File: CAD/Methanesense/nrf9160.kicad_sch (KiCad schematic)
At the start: 40 parts, among them J3 Conn_Coaxial, J4 Conn_Coaxial, J5 SIM_Card, J6 Conn_02x05_Odd_Even, J7 Conn_02x05_Odd_Even, Q2 FDS6892A, SW1 KMR223GLFG, SW2 JS202011JCQN, U6 nRF9161-SIXX, U8 USBLC6-4SC6, U9 TPS22917DBV

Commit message: WIP
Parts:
- removed J3: Conn_Coaxial, Connector_Coaxial:U.FL_Hirose_U.FL-R-SMT-1_Vertical, symbol Connector:Conn_Coaxial
- removed J5: SIM_Card, Connector_Card:microSIM_JAE_SF53S006VCBR2000, symbol Connector:SIM_Card
- removed R27: 120R, symbol Library:R
- removed U6: nRF9161-SIXX, PCM_nordic-lib-kicad-nrf9:LGA_9161_16.0x10.5mm, symbol PCM_nordic-lib-kicad-nrf9:nRF9161-SIXX
- added AE1: NN02-220, symbol Device:Antenna
- added AE2: YCGO009AA, symbol Device:Antenna
- added C1, C2: 1.7pF, Methanesense:C_0603_1608Metric, symbol Device:C
- added C4: 8.5pF, Methanesense:C_0603_1608Metric, symbol Device:C
- added C5: 15pF, Methanesense:C_0603_1608Metric, symbol Device:C
- added J2: Conn_Coaxial, Connector_Coaxial:U.FL_Hirose_U.FL-R-SMT-1_Vertical, symbol Connector:Conn_Coaxial
- added J3: 693043020611, Methanesense:693043020611, symbol 693043020611:693043020611
- added L1: 2.3nH, Methanesense:L_0603_1608Metric, symbol Device:L
- added L4: NP, Methanesense:L_0603_1608Metric, symbol Device:L
- added L5: 7.5NH, Methanesense:L_0603_1608Metric, symbol Device:L
- added L6: 1.6nH, Methanesense:L_0603_1608Metric, symbol Device:L
- added L7: 39NH, Methanesense:L_0603_1608Metric, symbol Device:L
- added L8: 68 nH, Methanesense:L_0603_1608Metric, symbol Device:L
- added R12, R13: 10k, Resistor_SMD:R_0603_1608Metric, symbol Library:R
- added U5: nRF9160-SICA, PCM_nordic-lib-kicad-nrf9:LGA_9160_16.0x10.5mm, symbol PCM_nordic-lib-kicad-nrf9:nRF9160-SIXX
- C21, C22: footprint (none) -> Capacitor_SMD:C_0805_2012Metric
- C23, C24, C25, C28, C29, C30, C31, C32, C33, C34, C35, C36, R18, R19, R20, R22, R23, R26: footprint (none) -> Capacitor_SMD:C_0603_1608Metric
- C26, C27: footprint (none) -> Methanesense:C_0603_1608Metric
- D5, D6: footprint (none) -> LED_SMD:LED_0603_1608Metric
- J6: value Conn_02x05_Odd_Even -> JLINK; footprint Connector_PinHeader_1.27mm:PinHeader_2x05_P1.27mm_Vertical_SMD -> esprelay:SEXY_pinpogo
- L2: value 39NH 250MA 0.7OHM SMD -> 39NH; footprint (none) -> Methanesense:L_0603_1608Metric
- R17, R24, R25: footprint (none) -> Resistor_SMD:R_0603_1608Metric
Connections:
- net ANT: now also C5.1, U5.61 (ANT)
- net COEX0: now also U5.93 (COEX0)
- net GND: now also C2.2, J2.2 (Ext), J3.C5 (GND), J3.S1, J3.S2, J3.S3, J3.S4, J3.S5, J3.S6, L4.2, L5.2, L7.2, U5.1 (GND_Shield), U5.103 (VSS), U5.11 (GND_Shield), U5.14 (GND_Shield), U5.17 (GND_Shield), U5.21 (GND_Shield), U5.27 (GND_Shield), U5.31 (GND_Shield), U5.36 (GND_Shield), U5.41 (GND_Shield), U5.44 (GND_Shield), U5.47 (GND_Shield), U5.5 (GND_Shield), U5.50 (GND_Shield), U5.52 (GND_Shield), U5.56 (GND_Shield), U5.6 (GND_Shield), U5.60 (GND_Shield), U5.62 (GND_Shield), U5.63 (GND_Shield), U5.65 (GND_Shield), U5.66 (GND_Shield), U5.68 (GND_Shield), U5.69 (GND_Shield), U5.7 (GND_Shield), U5.72 (GND_Shield), U5.74 (GND_Shield), U5.75 (GND_Shield), U5.76 (GND_Shield), U5.77 (GND_Shield), U5.78 (GND_Shield), U5.79 (GND_Shield), U5.8 (GND_Shield), U5.80 (GND_Shield), U5.81 (GND_Shield), U5.82 (GND_Shield), U5.85 (GND_Shield), U5.9 (GND_Shield), U5.90 (GND_Shield), U5.94 (GND_Shield), U5.98 (GND_Shield)
- net GPS: now also U5.67 (GPS)
- net P0.05: now also U5.2 (P0.05)
- net P0.06: now also U5.3 (P0.06)
- net P0.07: now also U5.4 (P0.07)
- net P0.08: now also U5.15 (P0.08)
- net P0.31: now also U5.89 (P0.31)
- net SIM_CLK: now also U5.46 (SIM_CLK)
- net SIM_IO: now also U8.1 (I/O1), U5.48 (SIM_IO); no longer U8.4 (I/O3)
- net SIM_RST: now also U8.4 (I/O3), U5.43 (SIM_RST); no longer U8.1 (I/O1)
- net SWDCLK: now also U5.33 (SWDCLK)
- net SWDIO: now also U5.34 (SWDIO)
- net SWO: now also U5.95 (P0.00)
- net ~{RESET}: now also U5.32 (~{RESET})
- net at C25.1: now also U5.13 (DEC0)
- net at R20.1: now also J3.C7 (I/O)
- net at R18.1: now also J3.C2 (RST)
- net at R19.1: now also J3.C3 (CLK)
- net +1V8 renamed +1V8SIM
- net +1V8SIM: now also J3.C1 (VCC), U5.49 (SIM_1V8)
- net ANT-: no longer names the net of C27.2, L2.1
- net ANT-: now also C1.1
- net GPS-: no longer names the net of C29.1, U9.6 (VOUT)
- net GPS-: now also L8.2; no longer C30.2, J4.1 (In)
- net QOD: no longer names the net of U9.5 (QOD)
- net VCC renamed +5V
- net +5V: now also U5.101 (ENABLE), U5.102 (VDD1), U5.22 (VDD2); no longer C23.1, C36.1
- net VDD renamed +2V0
- net +2V0: now also C23.1, C36.1, R12.2, R13.2, U5.12 (VDD_GPIO)
- new net: C1.2, L1.1
- new net: C2.1, C4.1, L1.2, L4.1
- new net: C5.2, J2.1 (In), L7.1
- new net: AE1.1 (A), L6.2
- new net: C4.2, L5.1, L6.1
- new net GPS_: C30.2, J4.1 (In), L8.1
- new net SCL: R13.1
- new net SDA: R12.1
- no-connect marks 15 -> 22
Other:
- moved on the sheet: C26, C27, C29, J6, L2

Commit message: Allmost there
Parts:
- removed R12, R13: 10k, Resistor_SMD:R_0603_1608Metric, symbol Library:R
- AE1: footprint (none) -> Methanesense:XCVR_NN02-220
- J6: now not fitted

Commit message: WIP
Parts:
- removed J7: Conn_02x05_Odd_Even, Connector_PinHeader_2.54mm:PinHeader_2x05_P2.54mm_Vertical, symbol Connector_Generic:Conn_02x05_Odd_Even
- added J5: Conn_01x10_Pin, Connector_PinHeader_2.54mm:PinHeader_1x10_P2.54mm_Vertical, symbol Connector:Conn_01x10_Pin
- C1, C2: MPN (none) -> GJM1555C1H1R7WB01
- C26, C27, C5: footprint Methanesense:C_0603_1608Metric -> Methanesense:C_0402_1005Metric_Sqr
- C29, C30: footprint Capacitor_SMD:C_0603_1608Metric -> Methanesense:C_0402_1005Metric_Sqr
- C4: MPN (none) -> GJM1555C1H8R5WB01
- J2, J4: MPN (none) -> HIROSE ELECTRIC U.FL-R-SMT-1
- J3: MPN (none) -> 693043020611
- L1: MPN (none) -> LQW15AN2N3G80
- L2, L7, L8: footprint Methanesense:L_0603_1608Metric -> Methanesense:C_0402_1005Metric_Sqr
- L5: MPN (none) -> LQW15AN7N5G80
- L6: MPN (none) -> LQW15AN1N6C80
- SW1: MPN (none) -> KMR223GLFG
- SW2: MPN (none) -> JS202011JCQN
- U5: MPN (none) -> nRF9160-SICA
- U8: MPN (none) -> USBLC6-4SC6
- U9: MPN (none) -> TPS22917DBV
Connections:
- net +2V0: now also J5.1 (Pin_1)
- net +5V: now also J5.2 (Pin_2)
- net +BATT: now also J5.3 (Pin_3)
- net GND: now also J5.4 (Pin_4), J5.6 (Pin_6)
- net P0.05: now also J5.9 (Pin_9)
- net P0.06: now also J5.8 (Pin_8)
- net P0.07: now also J5.7 (Pin_7)
- net P0.08: now also J5.10 (Pin_10)
- net P0.04: now reaches U5.100 (P0.04)
- net P0.09: now reaches U5.16 (P0.09)
- net P0.10: now reaches U5.18 (P0.10)
- net P0.11: now reaches U5.19 (P0.11)
- net P0.12: now reaches U5.20 (P0.12)
- net P0.13/AIN0: now reaches U5.23 (P0.13/AIN0)
- net P0.14/AIN1: now reaches U5.24 (P0.14/AIN1)
- net P0.15/AIN2: now reaches U5.25 (P0.15/AIN2)
- net P0.16/AIN3: now reaches U5.26 (P0.16/AIN3)
- net P0.17/AIN4: now reaches U5.28 (P0.17/AIN4)
- net P0.18/AIN5: now reaches U5.29 (P0.18/AIN5)
- net P0.19/AIN6: now reaches U5.30 (P0.19/AIN6)
- net P0.20/AIN7: now reaches U5.35 (P0.20/AIN7)
- net P0.26: now reaches U5.83 (P0.26)
- net P0.27: now reaches U5.84 (P0.27)
- net P0.28: now reaches U5.86 (P0.28)
- net P0.29: now reaches U5.87 (P0.29)
- net P0.30: now reaches U5.88 (P0.30)
- net P0.01: now reaches U5.96 (P0.01)
- net P0.02: now reaches U5.97 (P0.02)
- net P0.03: now reaches U5.99 (P0.03)
- new net +5VL: J5.5 (Pin_5)
- no-connect marks 22 -> 21
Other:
- moved on the sheet: C24, C28, R17

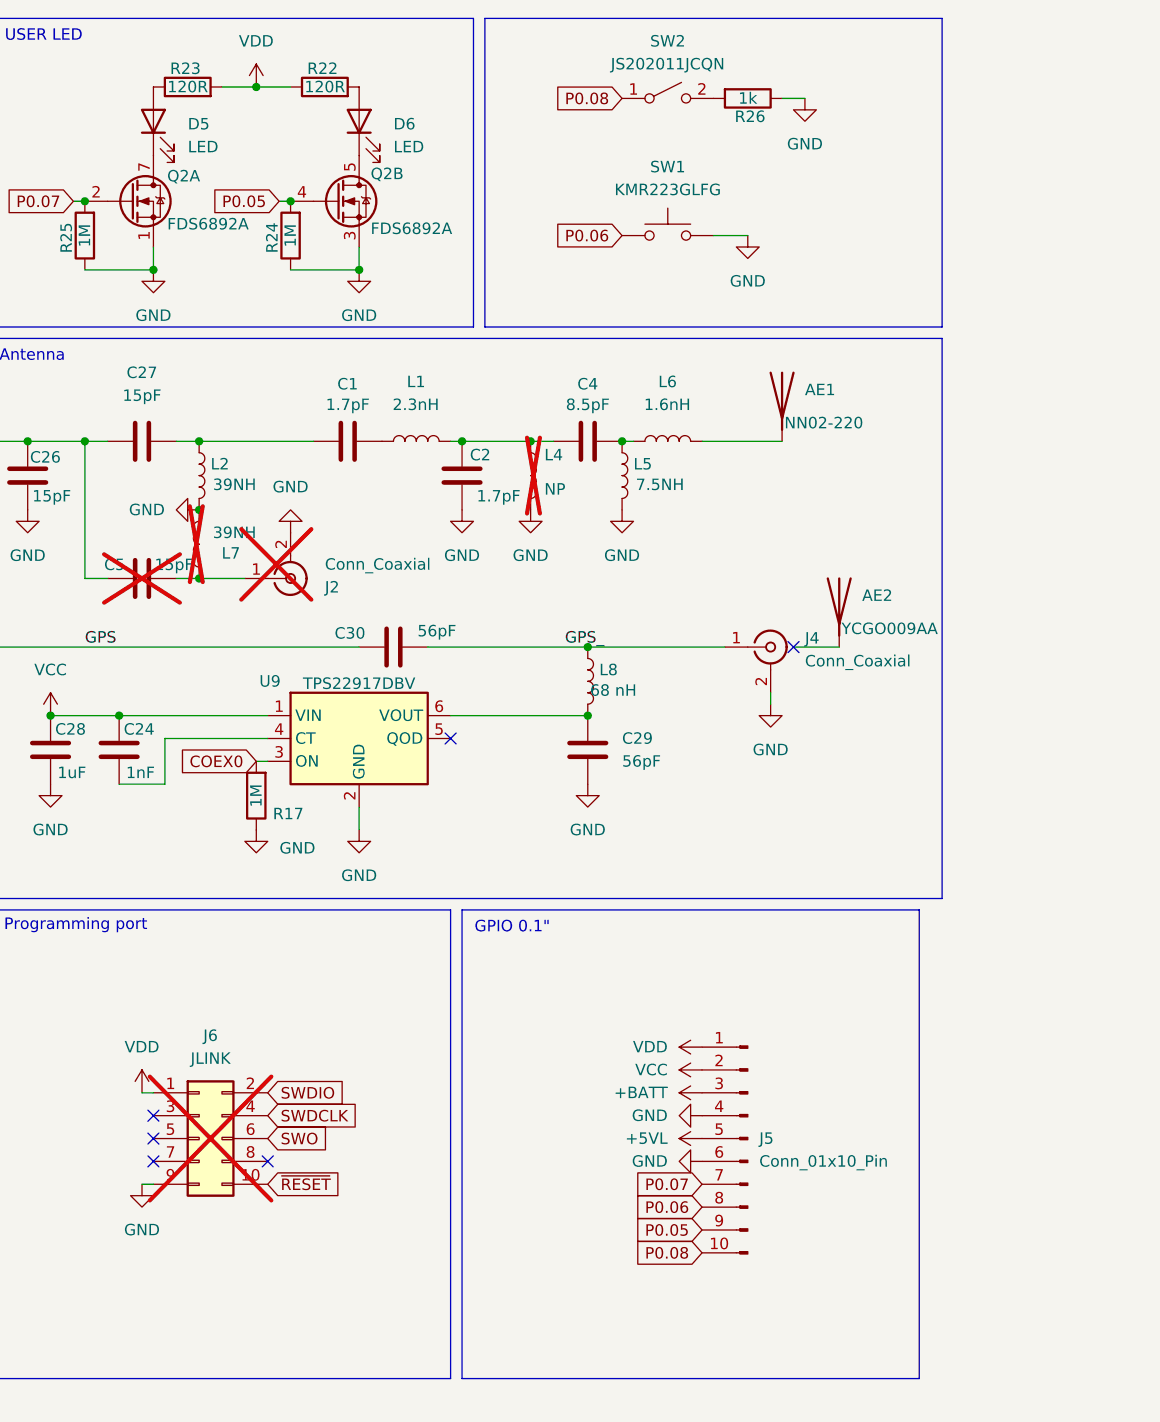
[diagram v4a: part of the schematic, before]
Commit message: NRF footprint change
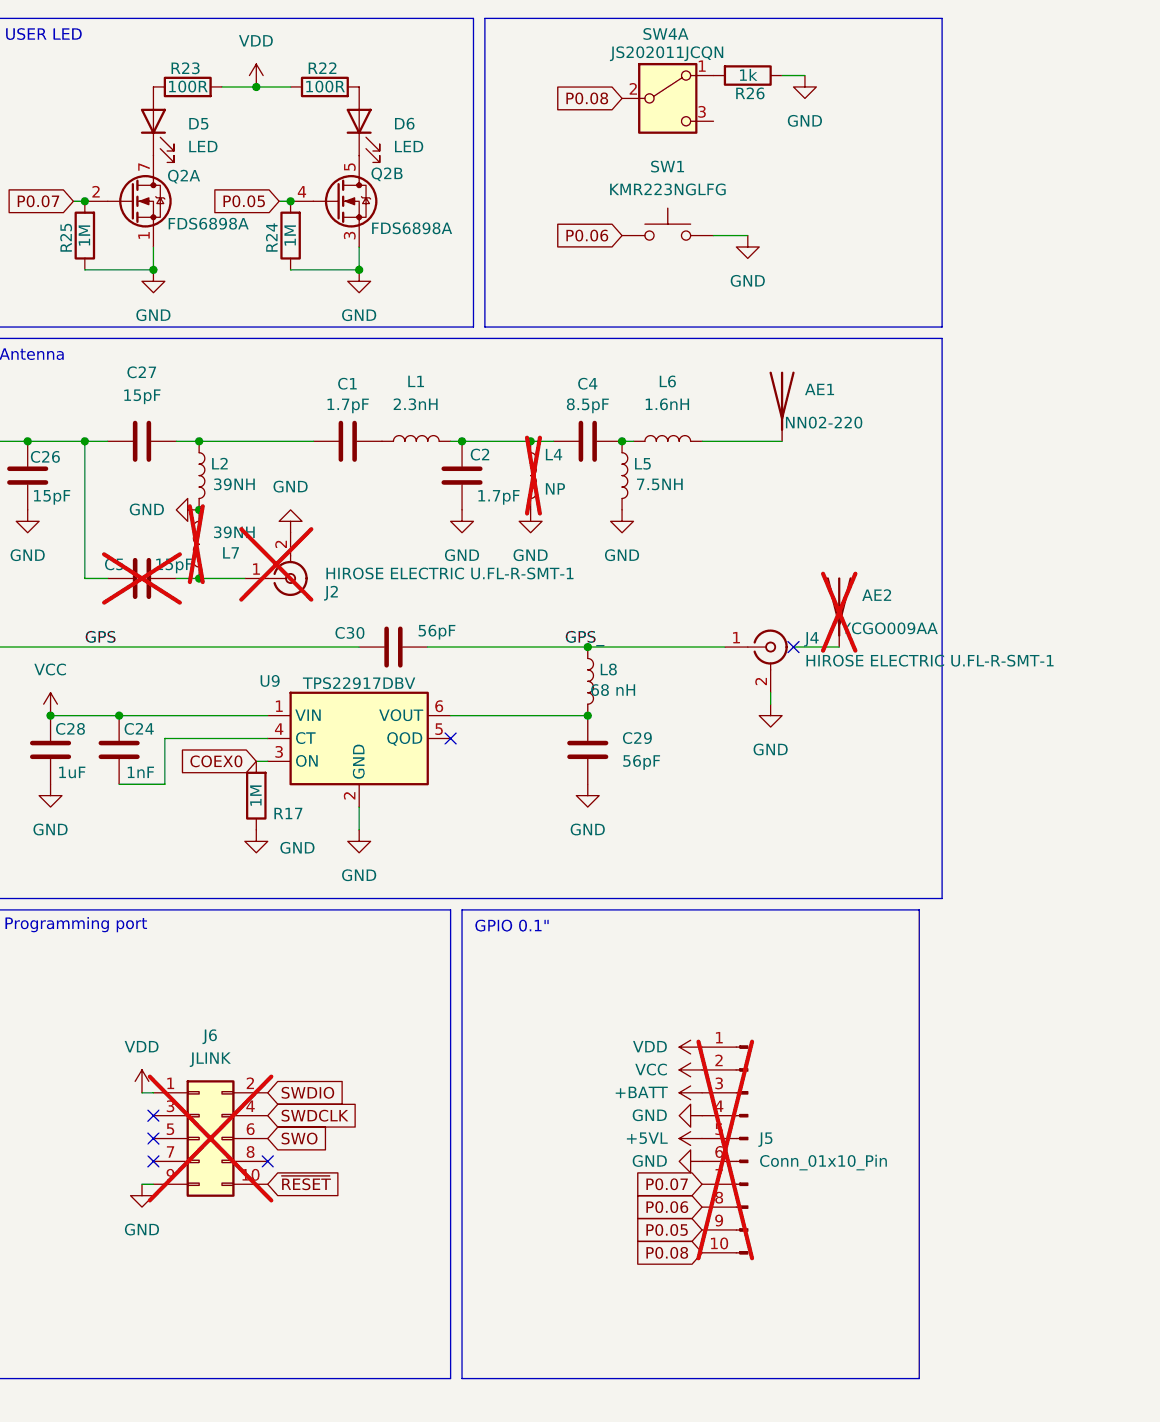
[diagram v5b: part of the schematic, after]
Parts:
- removed SW2: JS202011JCQN, Button_Switch_SMD:SW_DIP_SPSTx01_Slide_6.7x4.1mm_W6.73mm_P2.54mm_LowProfile_JPin, symbol Switch:SW_SPST
- added SW4: JS202011JCQN, Button_Switch_SMD:SW_DPDT_CK_JS202011JCQN, symbol Switch:SW_DPDT_x2
- AE1: MPN (none) -> NN02-220
- AE2, J5: now not fitted
- C26, C27, C5: MPN (none) -> GJM0335C1E150GB01D
- C29, C30: MPN (none) -> CBR04C560F1GAC
- C33, C35: footprint Capacitor_SMD:C_0603_1608Metric -> Methanesense:C_0402_1005Metric_Sqr; MPN (none) -> GJM0335C1E150GB01D
- D5, D6: MPN (none) -> LG L29K-G2J1-24-Z
- J2, J4: value Conn_Coaxial -> HIROSE ELECTRIC U.FL-R-SMT-1; footprint Connector_Coaxial:U.FL_Hirose_U.FL-R-SMT-1_Vertical -> Methanesense:U.FL_Hirose_U.FL-R-SMT-1_Vertical; MPN HIROSE ELECTRIC U.FL-R-SMT-1 -> U.FL-R-SMT-1
- J3: Package None -> (none)
- L2, L7: MPN (none) -> LQW15AN39NJ8ZD
- L8: MPN (none) -> LQW15AN68NG0ZD
- Q2: value FDS6892A -> FDS6898A; MPN (none) -> FDS6898A
- R18, R19, R20, R26: footprint Capacitor_SMD:C_0603_1608Metric -> Resistor_SMD:R_0603_1608Metric
- R22, R23: value 120R -> 100R; footprint Capacitor_SMD:C_0603_1608Metric -> Resistor_SMD:R_0603_1608Metric
- SW1: value KMR223GLFG -> KMR223NGLFG; footprint Button_Switch_SMD:SW_Push_1P1T_NO_CK_KMR2 -> Methanesense:SW_Push_1P1T_NO_CK_KMR2; MPN KMR223GLFG -> KMR223NGLFG
- U5: footprint PCM_nordic-lib-kicad-nrf9:LGA_9160_16.0x10.5mm -> Methanesense:LGA_9160_16.0x10.5mm; MPN nRF9160-SICA -> nRF9160-SICA-B1A-R7
- U9: MPN TPS22917DBV -> TPS22917DBVR
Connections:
- net P0.08: now also SW4.2 (B)
- net at R26.2: now also SW4.1 (A)
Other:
- moved on the sheet: R26

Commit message: Rev 2.0.0
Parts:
- C26, C27, C33, C35, C5: MPN GJM0335C1E150GB01D -> VJ0402D150FXCAJ
- R26, SW1, SW4: now not fitted
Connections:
- net GND: now also J6.3 (Pin_3), J6.5 (Pin_5), J6.7 (Pin_7), J6.8 (Pin_8)
- net P0.06: now also Q2.2 (G1), R25.2; no longer SW1.1
- net P0.07: now also SW1.1; no longer Q2.2 (G1), R25.2
- net P0.08: no longer J5.10 (Pin_10), SW4.2 (B)
- net P0.11: now also J5.10 (Pin_10), SW4.2 (B)
- no-connect marks 21 -> 17

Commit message: rev 1.2
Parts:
- removed C1, C2: 1.7pF, Methanesense:C_0603_1608Metric, symbol Device:C
- removed C4: 8.5pF, Methanesense:C_0603_1608Metric, symbol Device:C
- removed C5: 15pF, Methanesense:C_0402_1005Metric_Sqr, symbol Device:C
- removed D5, D6: LED, LED_SMD:LED_0603_1608Metric, symbol Device:LED
- removed J2: HIROSE ELECTRIC U.FL-R-SMT-1, Methanesense:U.FL_Hirose_U.FL-R-SMT-1_Vertical, symbol Connector:Conn_Coaxial
- removed J5: Conn_01x10_Pin, Connector_PinHeader_2.54mm:PinHeader_1x10_P2.54mm_Vertical, symbol Connector:Conn_01x10_Pin
- removed L1: 2.3nH, Methanesense:L_0603_1608Metric, symbol Device:L
- removed L4: NP, Methanesense:L_0603_1608Metric, symbol Device:L
- removed L5: 7.5NH, Methanesense:L_0603_1608Metric, symbol Device:L
- removed L6: 1.6nH, Methanesense:L_0603_1608Metric, symbol Device:L
- removed L7: 39NH, Methanesense:C_0402_1005Metric_Sqr, symbol Device:L
- removed R22, R23: 100R, Resistor_SMD:R_0603_1608Metric, symbol Library:R
- removed R26: 1k, Resistor_SMD:R_0603_1608Metric, symbol Library:R
- removed SW4: JS202011JCQN, Button_Switch_SMD:SW_DPDT_CK_JS202011JCQN, symbol Switch:SW_DPDT_x2
- added J1: HIROSE ELECTRIC U.FL-R-SMT-1, Methanesense:U.FL_Hirose_U.FL-R-SMT-1_Vertical, symbol Connector:Conn_Coaxial
- added J5: Conn_01x12_Pin, Connector_PinHeader_2.54mm:PinHeader_1x12_P2.54mm_Vertical, symbol Connector:Conn_01x12_Pin
- added R6: 0R, Resistor_SMD:R_0603_1608Metric, symbol Library:R
- AE1: value NN02-220 -> ~; footprint Methanesense:XCVR_NN02-220 -> (none); MPN NN02-220 -> (none); now not fitted
- J6, SW1: now fitted
- L8: value 68 nH -> 68 nH
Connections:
- net +2V0: now also J5.4 (Pin_4)
- net +BATT: now also J5.2 (Pin_2)
- net GND: now also J1.2 (Ext), J5.1 (Pin_1), J5.12 (Pin_12), J5.3 (Pin_3), J5.5 (Pin_5)
- net P0.01: now also Q2.4 (G2), R24.2
- net P0.04: now also SW1.1
- net P0.05: no longer Q2.4 (G2), R24.2
- net P0.06: no longer Q2.2 (G1), R25.2
- net P0.07: no longer SW1.1
- net P0.08: now also J5.6 (Pin_6)
- net P0.09: now also J5.7 (Pin_7)
- net P0.10: now also J5.8 (Pin_8)
- net P0.14/AIN1: now also J5.11 (Pin_11)
- net P0.17/AIN4: now also Q2.2 (G1), R25.2
- net P0.19/AIN6: now also J5.10 (Pin_10)
- net OD1: now reaches Q2.5 (D2), Q2.6 (D2)
- net OD2: now reaches Q2.7 (D1), Q2.8 (D1)
- net at C27.2, L2.1: now also R6.2
- net +5V renamed VCC
- net GPS: no longer names the net of C30.1, U5.67 (GPS)
- new net: J1.1 (In), R6.1
- new net P0.18/AIN5: J5.9 (Pin_9)
- no-connect marks 17 -> 18
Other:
- note added: "USER IO"
- note removed: "USER LED"
- moved on the sheet: C26, C27, L2

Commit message: Feat: Rev 1.3
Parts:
- removed J5: Conn_01x12_Pin, Connector_PinHeader_2.54mm:PinHeader_1x12_P2.54mm_Vertical, symbol Connector:Conn_01x12_Pin
- added D7: LG L29K-G2J1-24-Z, LED_SMD:LED_0603_1608Metric, symbol Device:LED
- added D8: MSS1P3L-M3/89A, Diode_SMD:D_MicroSMP_AK, symbol Device:D_Schottky
- added J5: Conn_01x13_Pin, Connector_PinHeader_2.54mm:PinHeader_1x13_P2.54mm_Vertical, symbol Connector:Conn_01x13_Pin
- added R29: 150R, Resistor_SMD:R_0603_1608Metric, symbol Library:R
- added R31, R32, R33: 0R, Resistor_SMD:R_0402_1005Metric, symbol Library:R
- added TP1: SWDIO, TestPoint:TestPoint_Pad_D1.0mm, symbol Connector:TestPoint
- added TP15: GND, TestPoint:TestPoint_Pad_D1.0mm, symbol Connector:TestPoint
- added TP2: SWDCLK, TestPoint:TestPoint_Pad_D1.0mm, symbol Connector:TestPoint
- added TP3: SWO, TestPoint:TestPoint_Pad_D1.0mm, symbol Connector:TestPoint
- added TP4: RST, TestPoint:TestPoint_Pad_D1.0mm, symbol Connector:TestPoint
- J6: MPN (none) -> BD125-10-A-0305-0580-L-B
- R6: footprint Resistor_SMD:R_0603_1608Metric -> Resistor_SMD:R_0402_1005Metric
- SW1: MPN KMR223NGLFG -> KMR223GLFG
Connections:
- net +2V0: now also J5.4 (Pin_4)
- net +BATT: now also J5.2 (Pin_2)
- net GND: now also D7.1 (K), J5.1 (Pin_1), J5.12 (Pin_12), J5.3 (Pin_3), J5.5 (Pin_5), R31.2, R32.2, TP15.1
- net P0.06: now also R29.2
- net P0.08: now also J5.6 (Pin_6)
- net P0.09: now also J5.7 (Pin_7)
- net P0.10: now also J5.8 (Pin_8)
- net P0.14/AIN1: now also J5.11 (Pin_11)
- net P0.18/AIN5: now also J5.9 (Pin_9)
- net P0.19/AIN6: now also J5.10 (Pin_10)
- net SWDCLK: now also TP2.1
- net SWDIO: now also TP1.1
- net SWO: now also TP3.1
- net ~{RESET}: now also TP4.1
- net at R6.1: now also R31.1, R33.1; no longer J1.1 (In)
- new net: D7.2 (A), R29.1
- new net: J1.1 (In), R32.1, R33.2
- new net +12V: D8.1 (K)
- new net 12vin: D8.2 (A), J5.13 (Pin_13)
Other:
- title: (none) -> NRF9160
- moved on the sheet: AE1, J1, J6, SW1
